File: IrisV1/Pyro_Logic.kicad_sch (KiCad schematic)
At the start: 25 parts, among them J14 TB002-500-02BE, J16 TB002-500-02BE, J21 TB002-500-02BE, J22 TB002-500-02BE, Q1 SI4909DY-T1-GE3, Q2 MBT3904DW1T1G

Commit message: Symbol changes to use common library in Iris
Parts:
- J14, J16, J21, J22: footprint screw terminal:CUI_TB002-500-02BE -> UNSW Rocketry Library:CUI_TB002-500-02BE; symbol screw terminal:TB002-500-02BE -> UNSW Rocketry library:TB002-500-02BE
- Q1: footprint pyro 1:SOIC_09DY-T1-GE3_VIS -> UNSW Rocketry Library:SOIC_09DY-T1-GE3_VIS; symbol PMOS MOSFET 1:SI4909DY-T1-GE3 -> UNSW Rocketry library:SI4909DY-T1-GE3
- Q2: footprint npn 1:SOT-363&slash_SC-88&slash_SC70-6&slash_CASE419B_OSI -> UNSW Rocketry Library:SOT-363&slash_SC-88&slash_SC70-6&slash_CASE419B_OSI; symbol NPN BJT 1:MBT3904DW1T1G -> UNSW Rocketry library:MBT3904DW1T1G
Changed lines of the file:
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@@
 	)
 	(symbol
-		(lib_id "PMOS MOSFET 1:SI4909DY-T1-GE3")
+		(lib_id "UNSW Rocketry library:SI4909DY-T1-GE3")
 		(at 217.17 95.25 0)
 		(unit 1)
@@
 			)
 		)
-		(property "Footprint" "pyro 1:SOIC_09DY-T1-GE3_VIS"
+		(property "Footprint" "UNSW Rocketry Library:SOIC_09DY-T1-GE3_VIS"
 			(at 217.17 95.25 0)
 			(hide yes)
@@
 	)
 	(symbol
-		(lib_id "NPN BJT 1:MBT3904DW1T1G")
+		(lib_id "UNSW Rocketry library:MBT3904DW1T1G")
 		(at 215.9 72.39 0)
 		(unit 1)
@@
 			)
 		)
-		(property "Footprint" "npn 1:SOT-363&slash_SC-88&slash_SC70-6&slash_CASE419B_OSI"
+		(property "Footprint" "UNSW Rocketry Library:SOT-363&slash_SC-88&slash_SC70-6&slash_CASE419B_OSI"
 			(at 215.9 72.39 0)
 			(hide yes)
@@
 	)
 	(symbol
-		(lib_id "screw terminal:TB002-500-02BE")
+		(lib_id "UNSW Rocketry library:TB002-500-02BE")
 		(at 241.3 148.59 0)
 		(mirror x)
@@
 			)
 		)
-		(property "Footprint" "screw terminal:CUI_TB002-500-02BE"
+		(property "Footprint" "UNSW Rocketry Library:CUI_TB002-500-02BE"
 			(at 241.3 148.59 0)
 			(hide yes)
@@
 	)
 	(symbol
-		(lib_id "screw terminal:TB002-500-02BE")
+		(lib_id "UNSW Rocketry library:TB002-500-02BE")
 		(at 160.02 78.74 0)
 		(mirror y)
@@
 			)
 		)
-		(property "Footprint" "screw terminal:CUI_TB002-500-02BE"
+		(property "Footprint" "UNSW Rocketry Library:CUI_TB002-500-02BE"
 			(at 160.02 78.74 0)
 			(hide yes)
@@
 	)
 	(symbol
-		(lib_id "screw terminal:TB002-500-02BE")
+		(lib_id "UNSW Rocketry library:TB002-500-02BE")
 		(at 242.57 158.75 0)
 		(unit 1)
@@
 			)
 		)
-		(property "Footprint" "screw terminal:CUI_TB002-500-02BE"
+		(property "Footprint" "UNSW Rocketry Library:CUI_TB002-500-02BE"
 			(at 242.57 158.75 0)
 			(hide yes)
@@
 	)
 	(symbol
-		(lib_id "screw terminal:TB002-500-02BE")
+		(lib_id "UNSW Rocketry library:TB002-500-02BE")
 		(at 176.53 26.67 0)
 		(unit 1)
@@
 			)
 		)
-		(property "Footprint" "screw terminal:CUI_TB002-500-02BE"
+		(property "Footprint" "UNSW Rocketry Library:CUI_TB002-500-02BE"
 			(at 176.53 26.67 0)
 			(hide yes)

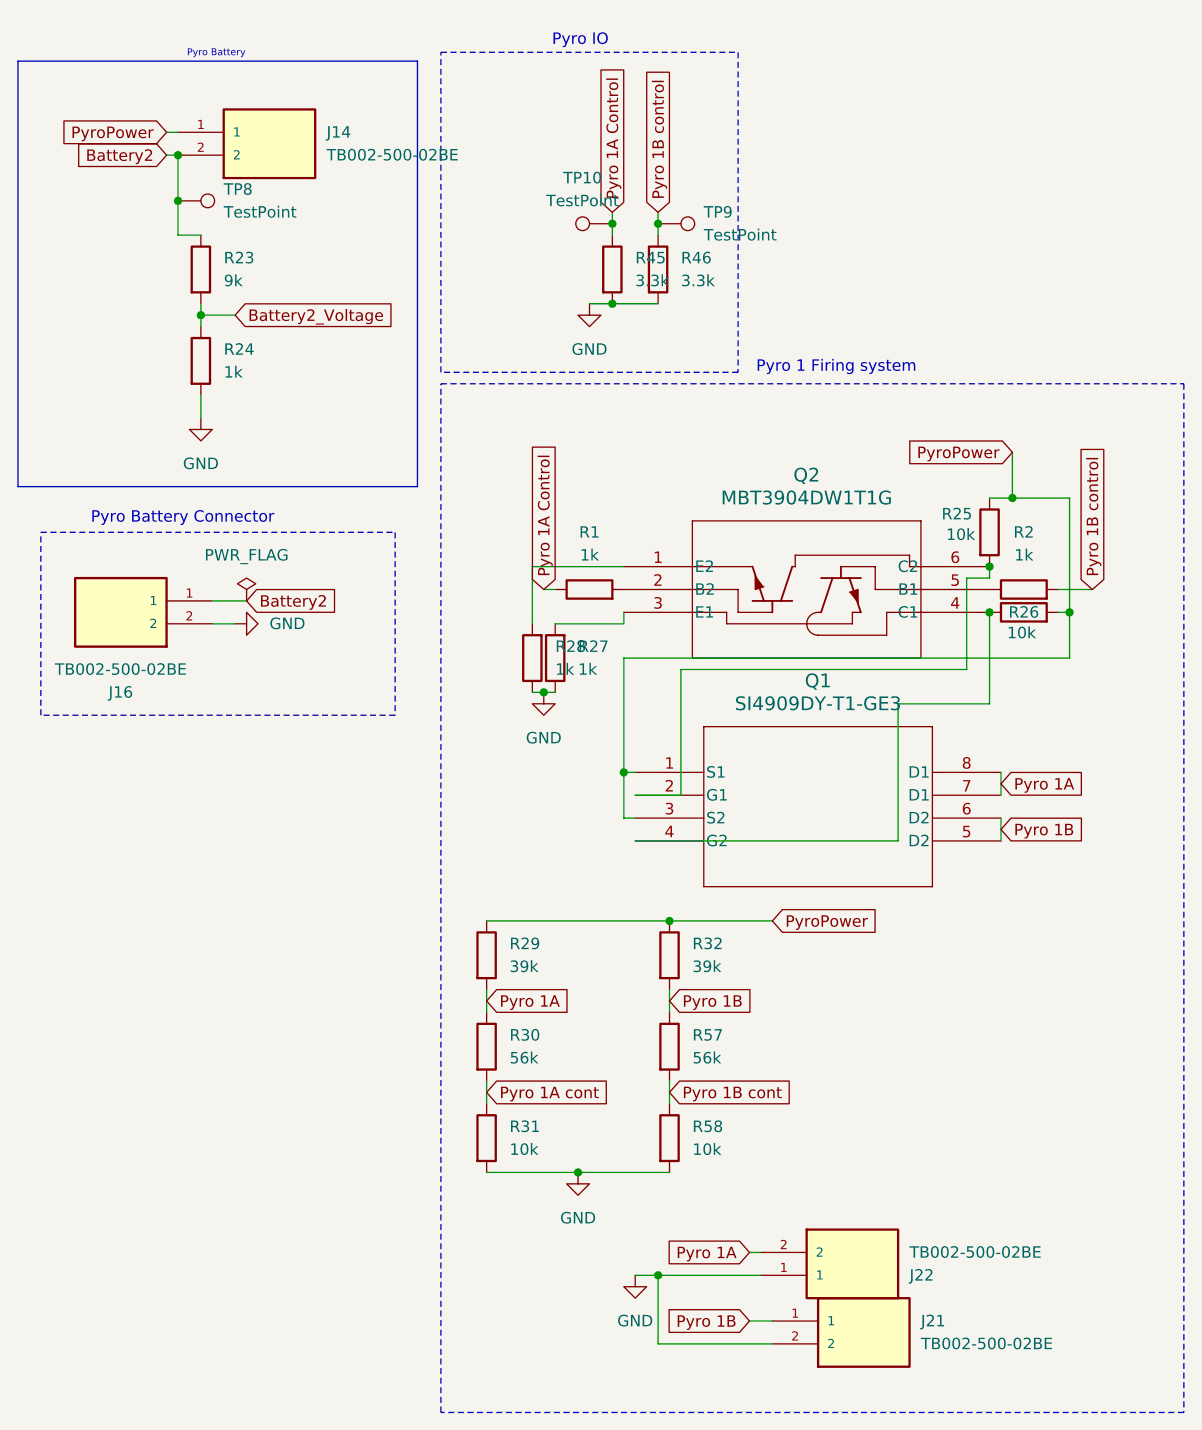
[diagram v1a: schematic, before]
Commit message: Changed to 3.5mm Screw terminals
All screw terminals in IRIS changed to 3.5mm screw terminals per Oliver's request.
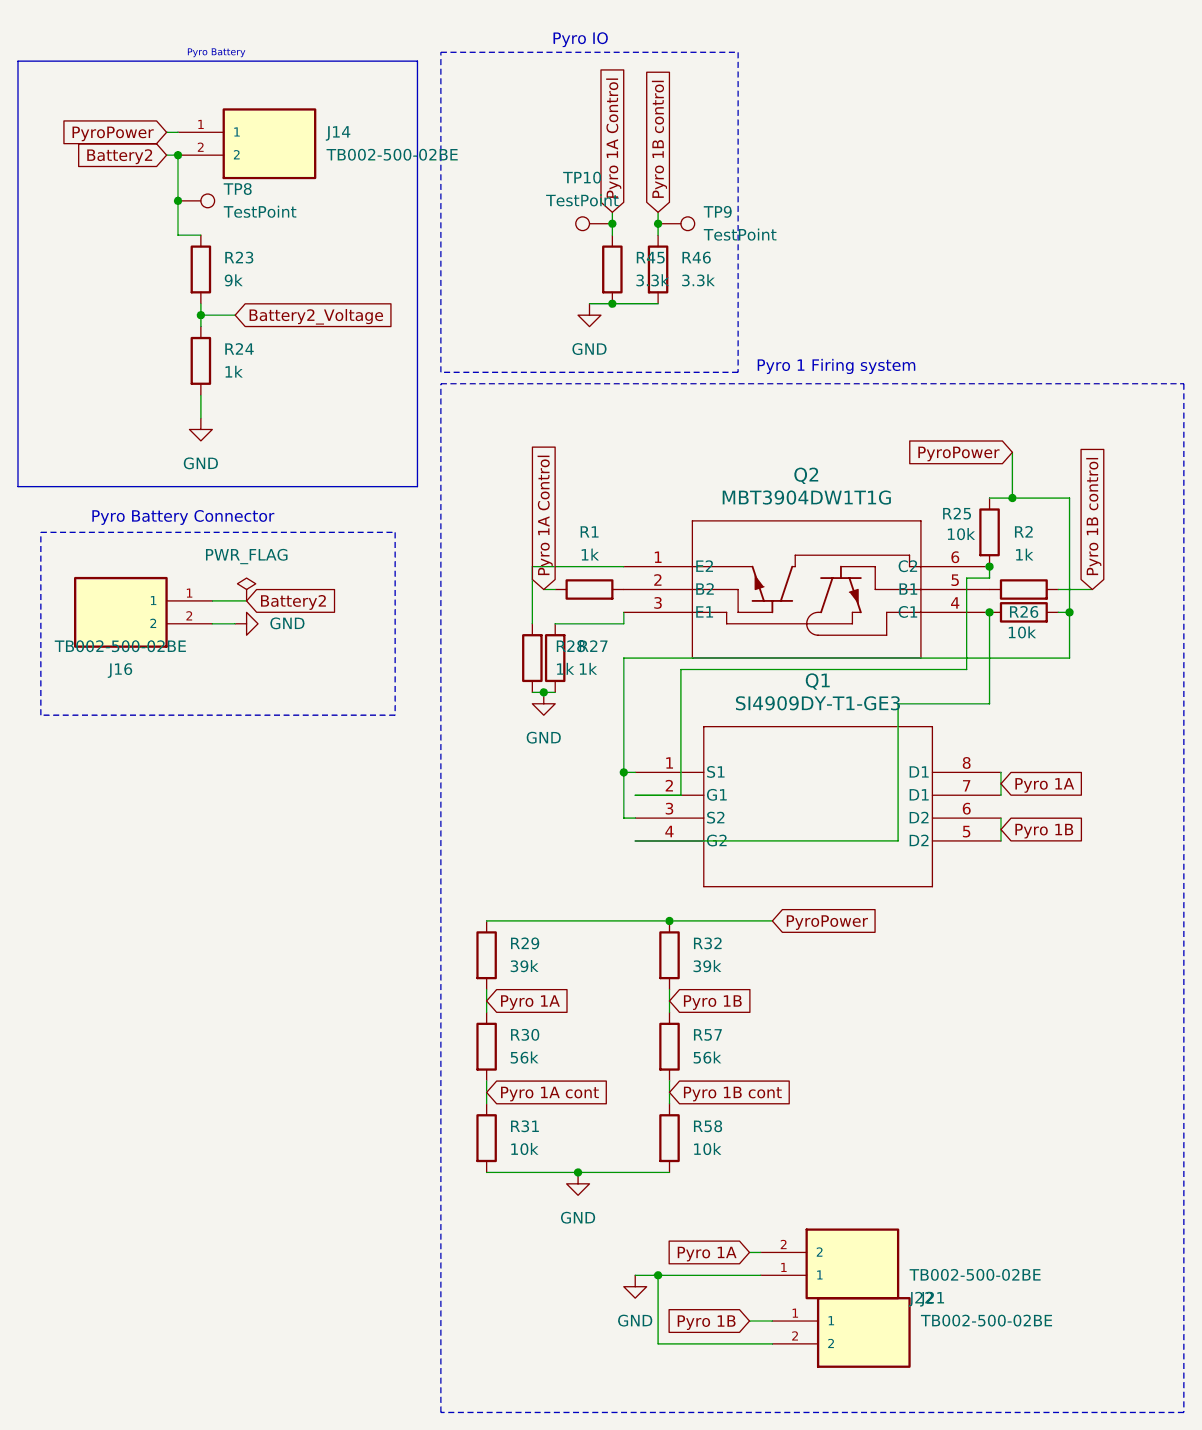
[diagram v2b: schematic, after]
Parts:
- J14, J16, J21, J22: footprint UNSW Rocketry Library:CUI_TB002-500-02BE -> UNSW Rocketry Library:ADAMTECH_EBWA-02-A; symbol UNSW Rocketry library:TB002-500-02BE -> UNSW Rocketry library:EBWA-02-A; MANUFACTURER CUI -> AdamTech; MAXIMUM_PACKAGE_HEIGHT (none) -> 8.5mm; PARTREV (none) -> A
